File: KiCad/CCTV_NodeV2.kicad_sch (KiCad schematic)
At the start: 9 parts, among them J1 Solar 6V/10W, J2 Battery (ext, 2× 18650 ||), U1 CN3791, U2 TC4056A_BMS, U3 MT3608, U4 ESP32-S3-DevKitC-1 N16R8, U5 OV7670

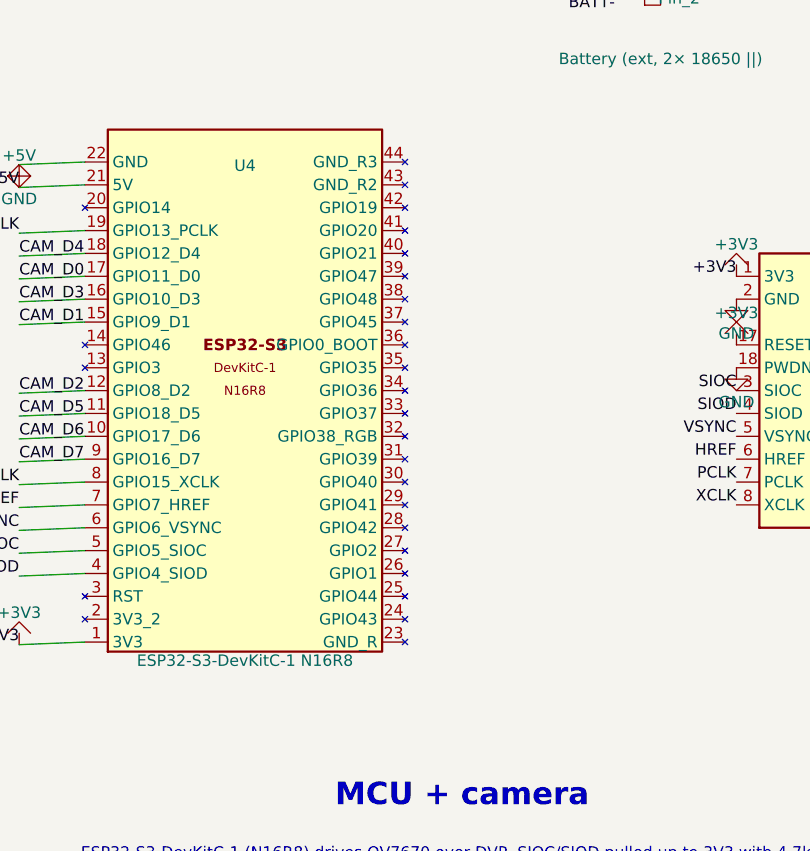
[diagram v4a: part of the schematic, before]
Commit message: Connect U4 right-column GND pins (23, 43, 44) to GND
The ESP32-S3-DevKitC-1 has 4 GND pads total:
  Pin 22 (left col, y=124.46)  — already connected via wire+symbol ✓
  Pin 23 (right col, y=177.80) — was unconnected ✗
  Pin 43 (right col, y=127.00) — was unconnected ✗
  Pin 44 (right col, y=124.46) — was unconnected ✗

Added GND power symbols at all three right-column GND pin
endpoints (x=101.60):
  Pin 23 → (101.6, 177.80)  [top of right column]
  Pin 43 → (101.6, 127.00)  [near bottom]
  Pin 44 → (101.6, 124.46)  [bottom]

All four GND pins now connected.
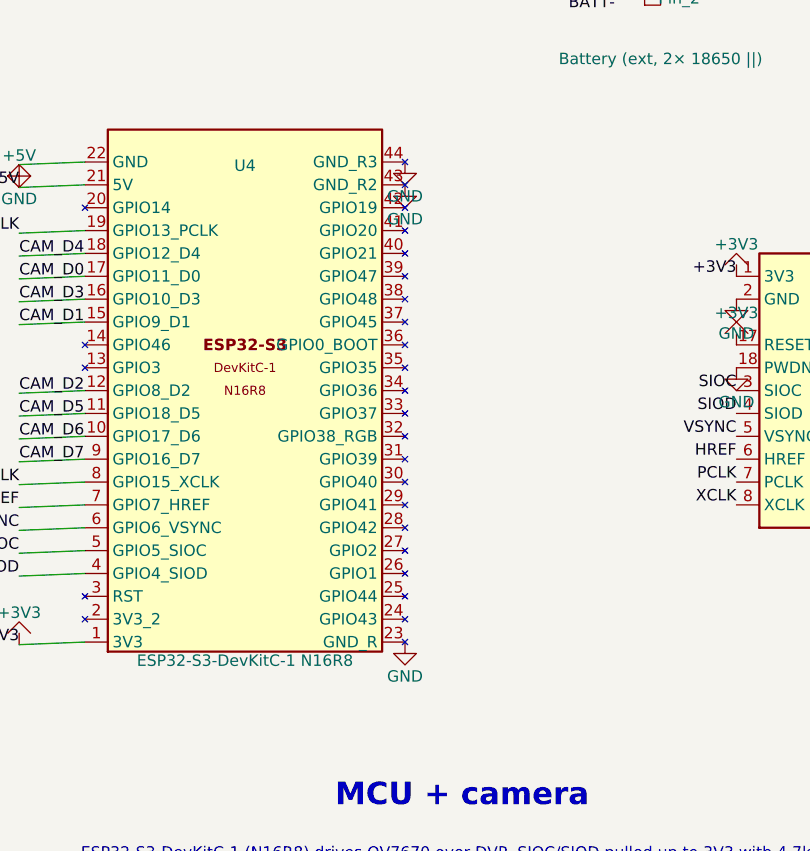
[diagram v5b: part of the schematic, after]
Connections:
- net GND: now also U4.23 (GND_R), U4.43 (GND_R2), U4.44 (GND_R3)
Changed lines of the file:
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@@
+		)
+	)
+	(symbol
+		(lib_id "CCTV2:GND")
+		(at 101.6 177.8 0)
+		(unit 1)
+		(body_style 1)
+		(exclude_from_sim no)
+		(in_bom yes)
+		(on_board yes)
+		(in_pos_files yes)
+		(dnp no)
+		(uuid "gnd0u4r-0023-0000-0000-000000000001")
+		(property "Reference" "#PWR_U4_R23"
+			(at 101.6 184.15 0)
+			(hide yes)
+			(show_name no)
+			(do_not_autoplace no)
+			(effects (font (size 1.27 1.27)))
+		)
+		(property "Value" "GND"
+			(at 101.6 181.61 0)
+			(show_name no)
+			(do_not_autoplace no)
+			(effects (font (size 1.27 1.27)))
+		)
+		(pin "1" (uuid "gnd0u4r-0023-0001-0000-000000000001"))
+		(instances
+			(project "CCTV_NodeV2"
+				(path "/b0c0d0e0-0001-4000-8000-000000000001"
+					(reference "#PWR_U4_R23")
+					(unit 1)
+				)
+			)
+		)
+	)
+	(symbol
+		(lib_id "CCTV2:GND")
+		(at 101.6 127.0 0)
+		(unit 1)
+		(body_style 1)
+		(exclude_from_sim no)
+		(in_bom yes)
+		(on_board yes)
+		(in_pos_files yes)
+		(dnp no)
+		(uuid "gnd0u4r-0043-0000-0000-000000000001")
+		(property "Reference" "#PWR_U4_R43"
+			(at 101.6 133.35 0)
+			(hide yes)
+			(show_name no)
+			(do_not_autoplace no)
+			(effects (font (size 1.27 1.27)))
+		)
+		(property "Value" "GND"
+			(at 101.6 130.81 0)
+			(show_name no)
+			(do_not_autoplace no)
+			(effects (font (size 1.27 1.27)))
+		)
+		(pin "1" (uuid "gnd0u4r-0043-0001-0000-000000000001"))
+		(instances
+			(project "CCTV_NodeV2"
+				(path "/b0c0d0e0-0001-4000-8000-000000000001"
+					(reference "#PWR_U4_R43")
+					(unit 1)
+				)
+			)
+		)
+	)
+	(symbol
+		(lib_id "CCTV2:GND")
+		(at 101.6 124.46 0)
+		(unit 1)
+		(body_style 1)
+		(exclude_from_sim no)
+		(in_bom yes)
+		(on_board yes)
+		(in_pos_files yes)
+		(dnp no)
+		(uuid "gnd0u4r-0044-0000-0000-000000000001")
+		(property "Reference" "#PWR_U4_R44"
+			(at 101.6 130.81 0)
+			(hide yes)
+			(show_name no)
+			(do_not_autoplace no)
+			(effects (font (size 1.27 1.27)))
+		)
+		(property "Value" "GND"
+			(at 101.6 128.27 0)
+			(show_name no)
+			(do_not_autoplace no)
+			(effects (font (size 1.27 1.27)))
+		)
+		(pin "1" (uuid "gnd0u4r-0044-0001-0000-000000000001"))
+		(instances
+			(project "CCTV_NodeV2"
+				(path "/b0c0d0e0-0001-4000-8000-000000000001"
+					(reference "#PWR_U4_R44")
+					(unit 1)
+				)
+			)
 		)
 	)
